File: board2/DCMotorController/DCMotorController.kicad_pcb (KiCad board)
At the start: 4 copper layers, 85 x 90 mm, 97 parts, among them J1 Conn_01x02, J2 Conn_01x02, M1_S1 Conn_01x03_Female, M1_S2 Conn_01x03_Female, Q1 Q_NMOS_GDS, Q2 Q_NMOS_GDS, Q3 Q_NMOS_GDS, Q4 Q_NMOS_GDS, Q5 Q_NMOS_GDS, Q6 Q_NMOS_GDS, Q7 Q_NMOS_GDS, Q8 Q_NMOS_GDS, U1 INA180A1, U10 TPS54360DDA, U2 IR2103, U3 IR2103, U4 ESP32-WROOM-32D, U9 DS18B20

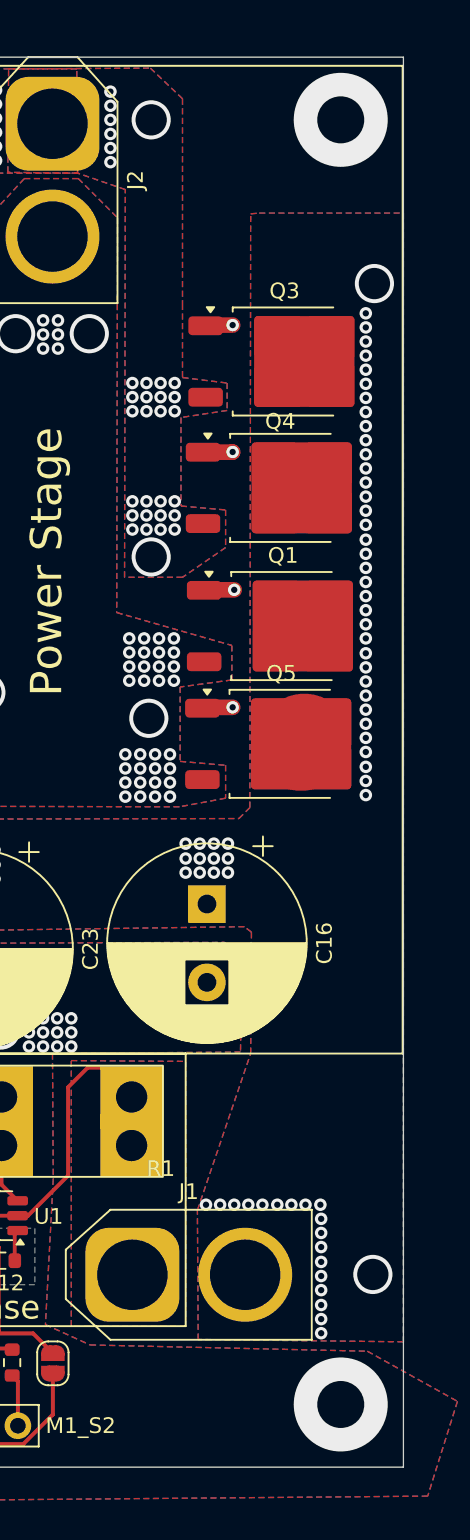
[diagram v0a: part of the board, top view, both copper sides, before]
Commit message: fix temp check wrong
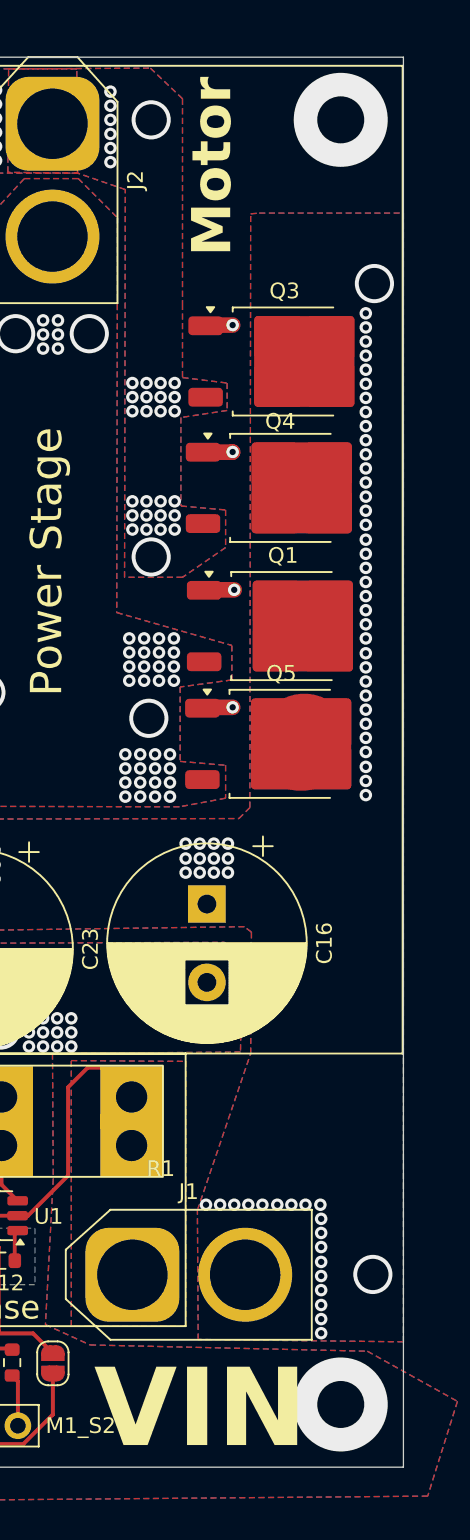
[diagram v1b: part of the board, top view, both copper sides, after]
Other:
- board text added: "Motor"
- board text added: "VIN"
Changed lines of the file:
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@@
+		)
+	)
+	(gr_text "VIN\n"
+		(at 115.25 106.7 0)
+		(layer "F.SilkS")
+		(effects
+			(font
+				(size 5 5)
+				(thickness 0.4)
+				(bold yes)
+			)
+			(justify left bottom)
+		)
+	)
+	(gr_text "Motor"
+		(at 124.25 30.2 90)
+		(layer "F.SilkS")
+		(effects
+			(font
+				(size 2.5 2.5)
+				(thickness 0.4)
+				(bold yes)
+			)
+			(justify left bottom)
 		)
 	)
